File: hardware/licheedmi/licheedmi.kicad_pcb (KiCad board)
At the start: 4 copper layers, 94 x 38 mm, 64 parts, among them J1 Conn_01x07, J2 HDMI_A_PCB, J3 LicheePiNano_LCD, J4 HDMI_A, U1 TDA19988, U2 LicheeNano, U3 TS3DV20812, U4 SC6206B

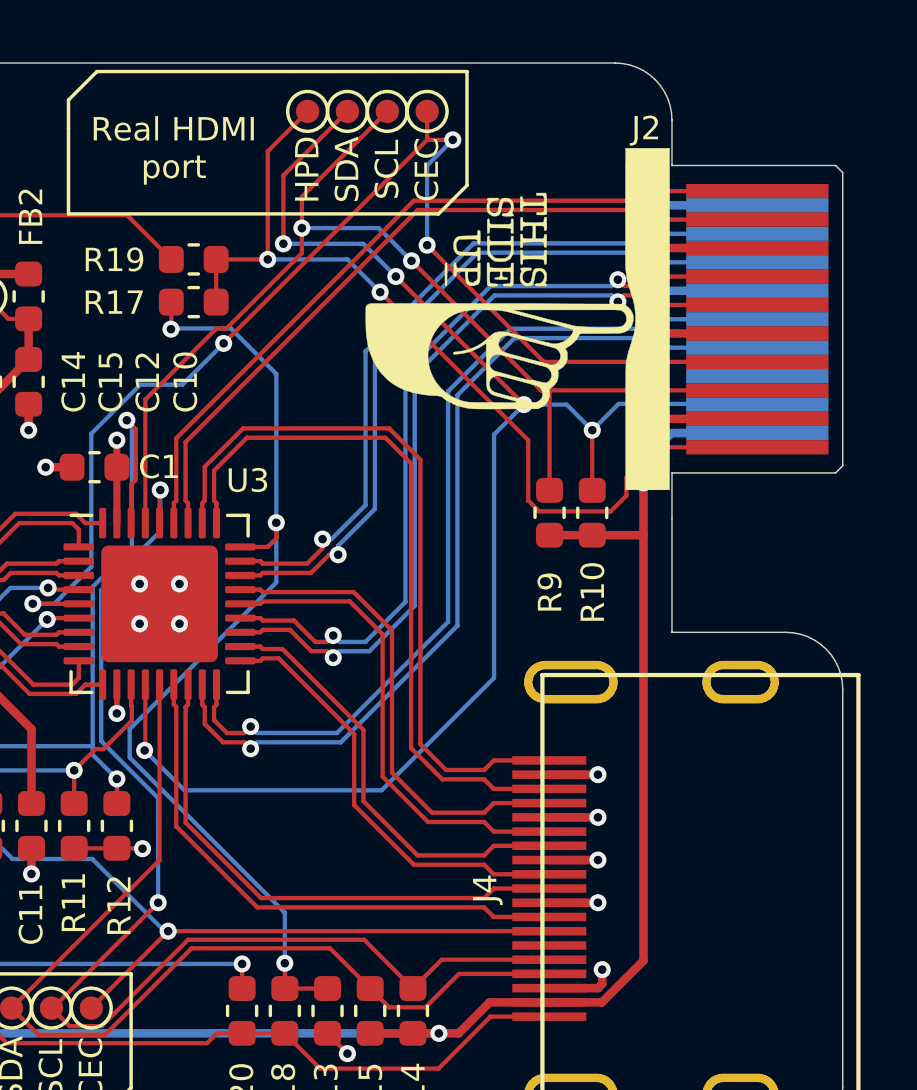
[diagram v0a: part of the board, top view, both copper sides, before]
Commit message: pcb: Length and skew tuned HDMI pairs
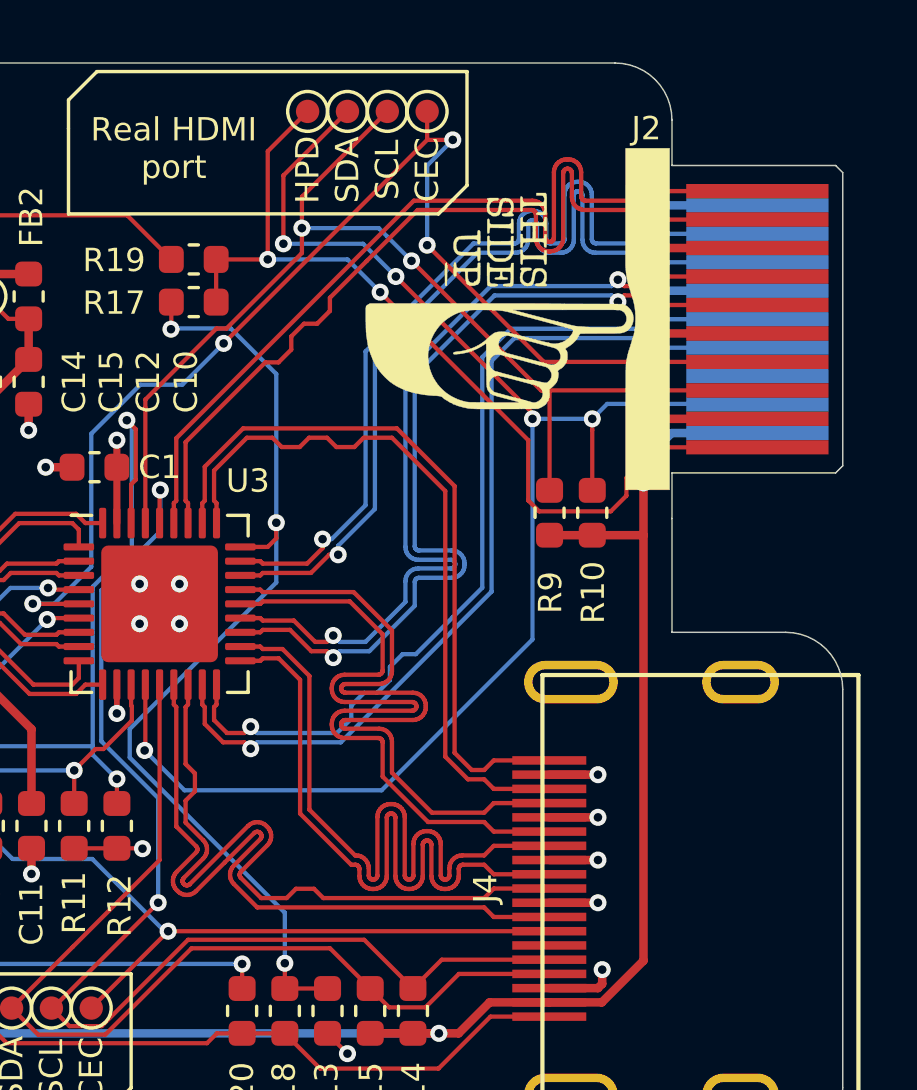
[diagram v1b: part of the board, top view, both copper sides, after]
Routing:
- net /HD0_FEM_P: track 15.5 -> 25.6 mm
- net /HD0_FEM_N: track 15.5 -> 25.6 mm
- net /HD1_FEM_N: track 17.2 -> 25.6 mm
- net /HD1_FEM_P: track 17.2 -> 25.6 mm
- net /HDC_FEM_P: track 18.9 -> 25.6 mm
- net /HDC_FEM_N: track 19.4 -> 25.6 mm
- net /HD1_PCB_P: track 26.4 -> 31.9 mm
- net /HD1_PCB_N: track 26.4 -> 31.9 mm
- net /HD2_PCB_N: track 26.5 -> 32.1 mm
- net /HD2_PCB_P: track 27.0 -> 32.1 mm
- net /HD0_PCB_P: track 29.0 -> 31.9 mm
- net /HD0_PCB_N: track 29.0 -> 31.9 mm
- net /HDC_PCB_P: track 31.5 -> 32.1 mm
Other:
- board text added: "A"
- board text added: "PCB HDMI length target: 32.07mm Real HDMI length target: 25.645mm"
- board text added: "S"
- board text added: "S'"
- board text added: "S1"
- board text added: "S1 < 2S' A = S' + w S = 4w + 2S'"
- board text added: "W"
- board text added: "w = 0.1524 S' = 0.175 => A = 0.3274 => S = 0.9596"

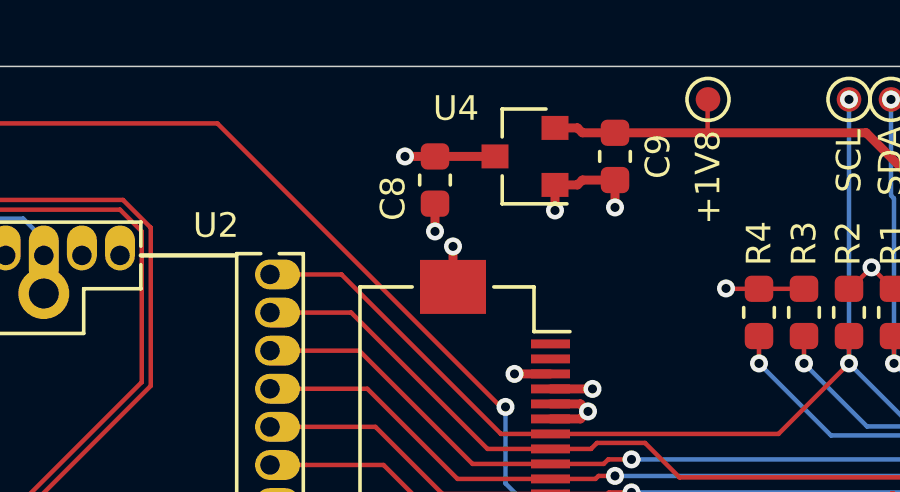
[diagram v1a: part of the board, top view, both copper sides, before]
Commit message: pcb: Changed layer 3 from +3V3 to GND
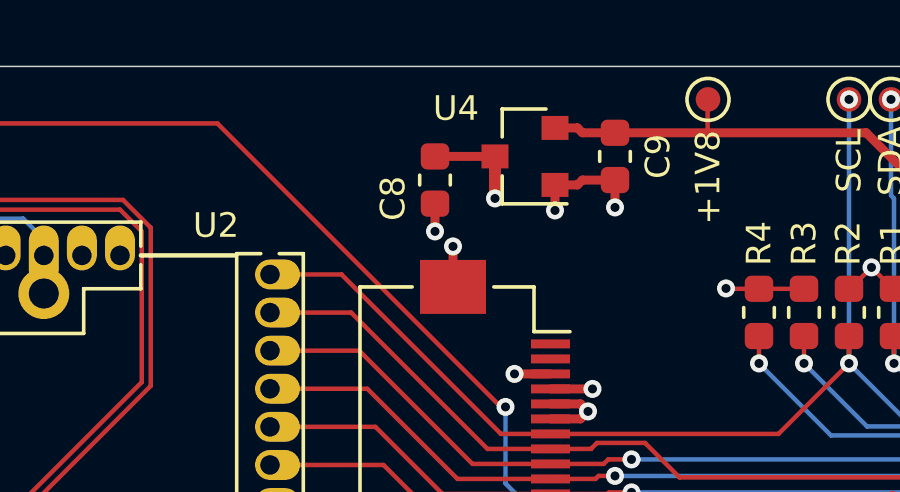
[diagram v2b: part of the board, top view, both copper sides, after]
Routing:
- net +3V3: track 25.6 -> 163.3 mm
- added copper zone on In2.Cu, net GND
- removed copper zone on In2.Cu, net +3V3
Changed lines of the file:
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@@
     (thickness 0.8)
     (drawings 93)
-    (tracks 1834)
+    (tracks 1861)
     (zones 0)
     (modules 64)
@@
   )
   (setup
-    (last_trace_width 0.15)
+    (last_trace_width 0.4)
     (user_trace_width 0.15)
     (user_trace_width 0.2)
@@
   (segment (start 158.69 103.5) (end 160.4 103.5) (width 0.3) (layer F.Cu) (net 1))
   (segment (start 114 74) (end 116 74) (width 0.3) (layer F.Cu) (net 2))
-  (via (at 113 74) (size 0.6) (drill 0.3) (layers F.Cu B.Cu) (net 2))
-  (segment (start 114 74) (end 113 74) (width 0.3) (layer F.Cu) (net 2))
   (segment (start 142 98.5875) (end 143.5 98.5875) (width 0.15) (layer F.Cu) (net 2))
   (via (at 144.4 98.6) (size 0.6) (drill 0.3) (layers F.Cu B.Cu) (net 2))
@@
   (segment (start 87.2 106.4875) (end 88.2875 106.4875) (width 0.3) (layer F.Cu) (net 2))
   (segment (start 88.2875 106.4875) (end 88.3 106.5) (width 0.3) (layer F.Cu) (net 2))
+  (segment (start 90.8 77.3) (end 90.8 78.57) (width 0.4) (layer In2.Cu) (net 2))
+  (segment (start 90.8 78.57) (end 90.8 83.8) (width 0.4) (layer In2.Cu) (net 2))
+  (segment (start 90.8 83.8) (end 105.7 98.7) (width 0.4) (layer In2.Cu) (net 2))
+  (segment (start 105.7 98.7) (end 105.7 104.7) (width 0.4) (layer In2.Cu) (net 2))
+  (segment (start 103.9 106.5) (end 88.3 106.5) (width 0.4) (layer In2.Cu) (net 2))
+  (segment (start 105.7 104.7) (end 103.9 106.5) (width 0.4) (layer In2.Cu) (net 2))
+  (segment (start 105.7 104.7) (end 113.1 104.7) (width 0.4) (layer In2.Cu) (net 2))
+  (segment (start 116 101.8) (end 116 95.3) (width 0.4) (layer In2.Cu) (net 2))
+  (segment (start 113.1 104.7) (end 116 101.8) (width 0.4) (layer In2.Cu) (net 2))
+  (segment (start 116 95.3) (end 116 89.4) (width 0.4) (layer In2.Cu) (net 2))
+  (segment (start 116 89.4) (end 117.9 87.5) (width 0.4) (layer In2.Cu) (net 2))
+  (via (at 116 75.4) (size 0.6) (drill 0.3) (layers F.Cu B.Cu) (net 2))
+  (segment (start 117.9 77.3) (end 116 75.4) (width 0.4) (layer In2.Cu) (net 2))
+  (segment (start 116 75.4) (end 116 74) (width 0.4) (layer F.Cu) (net 2))
+  (segment (start 117.95 81.75) (end 117.9 81.8) (width 0.4) (layer In2.Cu) (net 2))
+  (segment (start 119.25 81.75) (end 117.95 81.75) (width 0.4) (layer In2.Cu) (net 2))
+  (segment (start 117.9 87.5) (end 117.9 81.8) (width 0.4) (layer In2.Cu) (net 2))
+  (segment (start 117.9 81.8) (end 117.9 77.3) (width 0.4) (layer In2.Cu) (net 2))
+  (segment (start 119.25 81.75) (end 122.45 81.75) (width 0.4) (layer In2.Cu) (net 2))
+  (segment (start 126.5 77.7) (end 128.55 77.7) (width 0.4) (layer In2.Cu) (net 2))
+  (segment (start 122.45 81.75) (end 126.5 77.7) (width 0.4) (layer In2.Cu) (net 2))
+  (segment (start 128.55 77.7) (end 138.2 77.7) (width 0.4) (layer In2.Cu) (net 2))
+  (segment (start 138.2 77.7) (end 141.3 80.8) (width 0.4) (layer In2.Cu) (net 2))
+  (segment (start 141.3 82.05) (end 143.5 84.25) (width 0.4) (layer In2.Cu) (net 2))
+  (segment (start 141.3 80.8) (end 141.3 82.05) (width 0.4) (layer In2.Cu) (net 2))
+  (segment (start 142.8 87.8) (end 142.8 97) (width 0.4) (layer In2.Cu) (net 2))
+  (segment (start 143.5 84.25) (end 143.5 87.1) (width 0.4) (layer In2.Cu) (net 2))
+  (segment (start 142.8 97) (end 144.4 98.6) (width 0.4) (layer In2.Cu) (net 2))
+  (segment (start 143.5 87.1) (end 142.8 87.8) (width 0.4) (layer In2.Cu) (net 2))
   (segment (start 133.75 85.5875) (end 133.75 83.9) (width 0.2) (layer F.Cu) (net 3))
   (segment (start 128.5875 92.75) (end 126.9 92.75) (width 0.2) (layer F.Cu) (net 3))
@@
   (segment (start 156.403699 97.6637) (end 156.739999 98) (width 0.1524) (layer F.Cu) (net 69))
   (segment (start 154.432192 97.6637) (end 156.403699 97.6637) (width 0.1524) (layer F.Cu) (net 69))
-  (segment (start 152.8363 94.8651) (end 152.8363 96.067808) (width 0.1524) (layer F.Cu) (net 69))
   (segment (start 152.750023 94.727792) (end 152.778919 94.745948) (width 0.1524) (layer F.Cu) (net 69))
   (segment (start 151.501019 94.7127) (end 152.6839 94.7127) (width 0.1524) (layer F.Cu) (net 69))
@@
   (segment (start 151.093713 93.192372) (end 151.147572 93.278088) (width 0.1524) (layer F.Cu) (net 69))
   (segment (start 151.147572 93.278088) (end 151.219155 93.349671) (width 0.1524) (layer F.Cu) (net 69))
+  (segment (start 152.8363 94.8651) (end 152.8363 96.067808) (width 0.1524) (layer F.Cu) (net 69))
   (segment (start 151.46262 94.095592) (end 151.433724 94.113748) (width 0.1524) (layer F.Cu) (net 70))
   (segment (start 151.494831 94.08432) (end 151.46262 94.095592) (width 0.1524) (layer F.Cu) (net 70))
@@
   (segment (start 147.8375 89.5) (end 148.5375 89.5) (width 0.1524) (layer F.Cu) (net 70))
   (segment (start 151.817808 89.5863) (end 153.1637 90.932192) (width 0.1524) (layer F.Cu) (net 70))
-  (segment (start 153.1637 94.837375) (end 153.1637 95.932192) (width 0.1524) (layer F.Cu) (net 70))
   (segment (start 151.46262 92.831192) (end 151.433724 92.849348) (width 0.1524) (layer F.Cu) (net 70))
   (segment (start 153.1637 90.932192) (end 153.1637 92.364024) (width 0.1524) (layer F.Cu) (net 70))
@@
   (segment (start 156.403699 97.3363) (end 156.739999 97) (width 0.1524) (layer F.Cu) (net 70))
   (segment (start 156.739999 97) (end 158.69 97) (width 0.1524) (layer F.Cu) (net 70))
+  (segment (start 153.1637 94.837375) (end 153.1637 95.932192) (width 0.1524) (layer F.Cu) (net 70))
   (segment (start 156.403699 96.1637) (end 156.739999 96.5) (width 0.1524) (layer F.Cu) (net 71))
   (segment (start 155.832192 96.1637) (end 156.403699 96.1637) (width 0.1524) (layer F.Cu) (net 71))
@@
     (polygon
       (pts
-        (xy 164 110) (xy 73 110) (xy 73 69) (xy 164 69)
+        (xy 171 110) (xy 73 110) (xy 73 69) (xy 171 69)
       )
     )
   )
-  (zone (net 2) (net_name +3V3) (layer In2.Cu) (hatch edge 0.508)
+  (zone (net 1) (net_name GND) (layer In2.Cu) (hatch edge 0.508)
     (connect_pads (clearance 0.15))
     (min_thickness 0.15)
@@
     (polygon
       (pts
-        (xy 164 111) (xy 74 111) (xy 74 70) (xy 164 70)
+        (xy 172 111) (xy 74 111) (xy 74 70) (xy 172 70)
+      )
+    )
+  )
+  (zone (net 0) (net_name "") (layers In1.Cu In2.Cu) (hatch edge 0.508)
+    (connect_pads (clearance 0.15))
+    (min_thickness 0.15)
+    (keepout (tracks allowed) (vias allowed) (copperpour not_allowed))
+    (fill (arc_segments 32) (thermal_gap 0.16) (thermal_bridge_width 0.2))
+    (polygon
+      (pts
+        (xy 170 86) (xy 164 86) (xy 164 74) (xy 170 74)
       )
     )

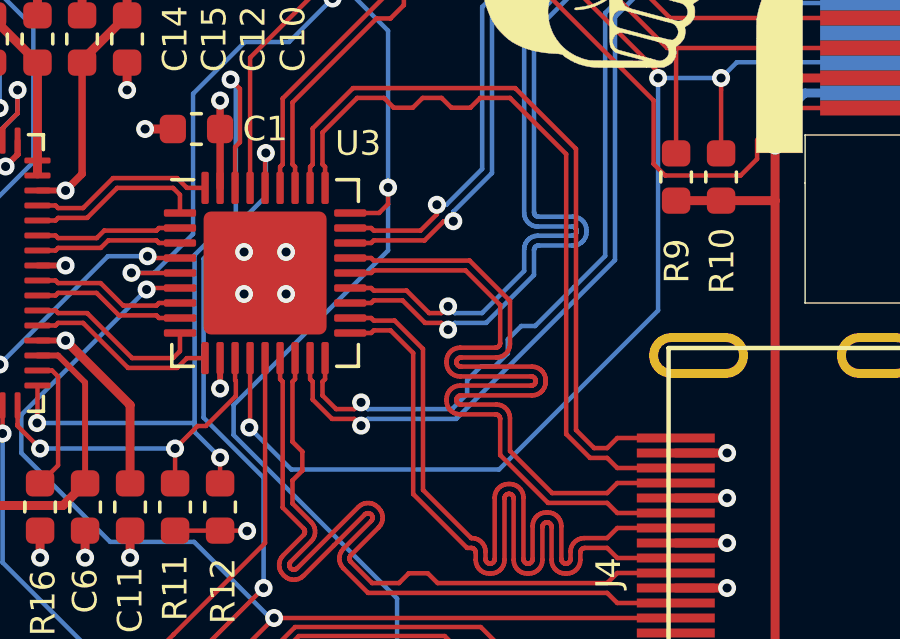
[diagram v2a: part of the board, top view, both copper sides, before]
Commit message: pcb: Add proper diff pair layer transition vias
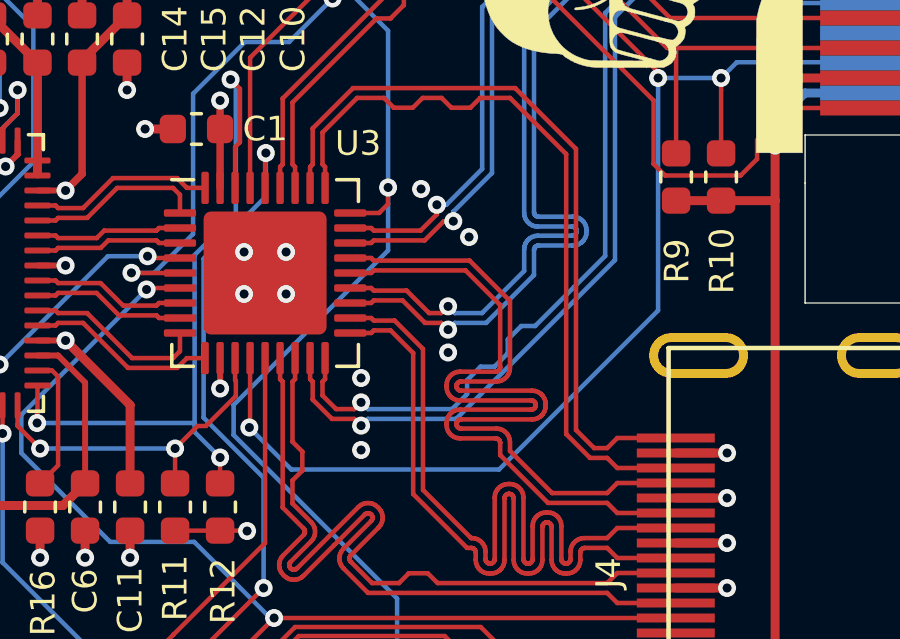
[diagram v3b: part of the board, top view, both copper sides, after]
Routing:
- net GND: vias 57 -> 62
